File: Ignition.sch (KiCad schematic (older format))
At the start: 16 parts, among them Q1 Q_PMOS_GDS, Q2 Q_NMOS_GDS, Q3 Q_NMOS_GDS, Q4 Q_NMOS_GDS, Q5 Q_PMOS_GDS, Q6 Q_PMOS_GDS

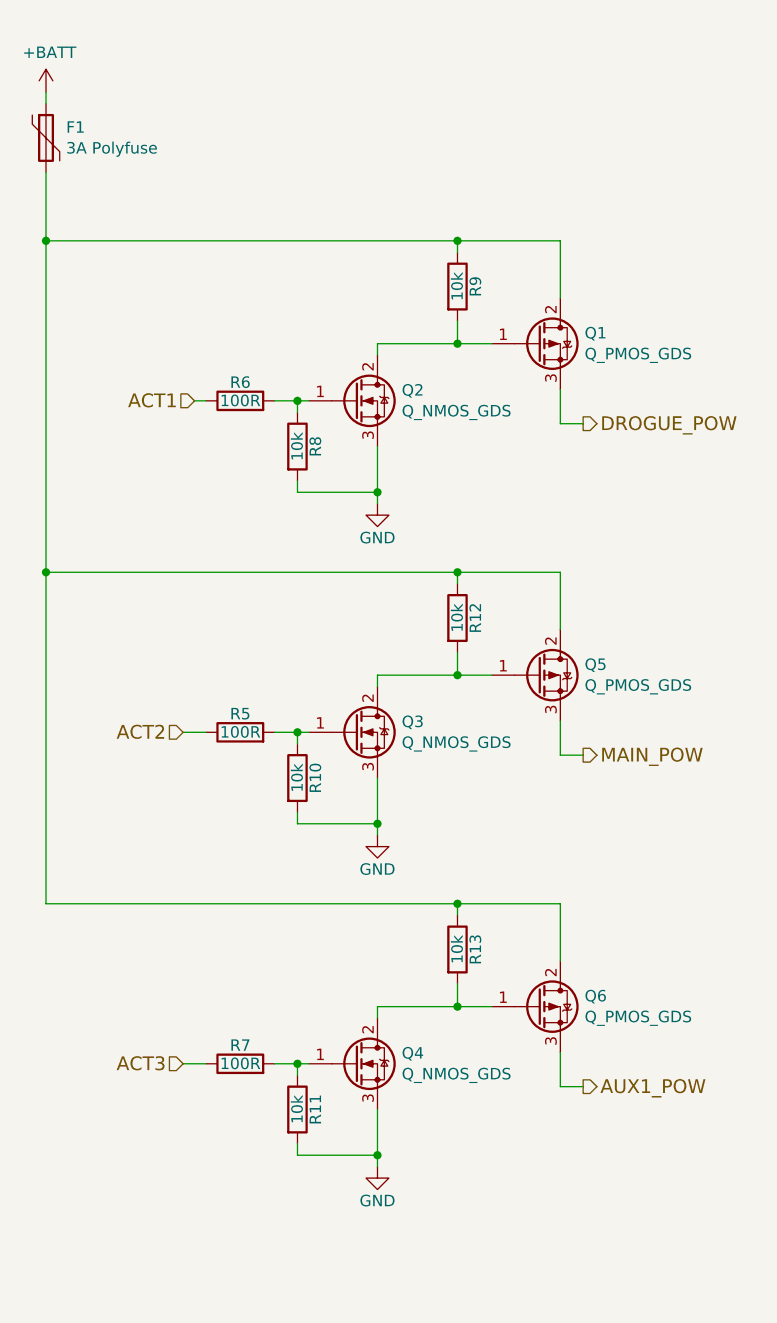
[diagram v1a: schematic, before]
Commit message: Added 10R series termination resistors to high-speed digital lines Added reverse-power protection diode Added ADC filter capacitors Added I2C pullups Added individual polyfuses to pyro drivers Changed UBSEDS logo to smaller variant Reduced LED resistors to 470R Reduced most SMD footprints to 0603 Minor schematic cleanup
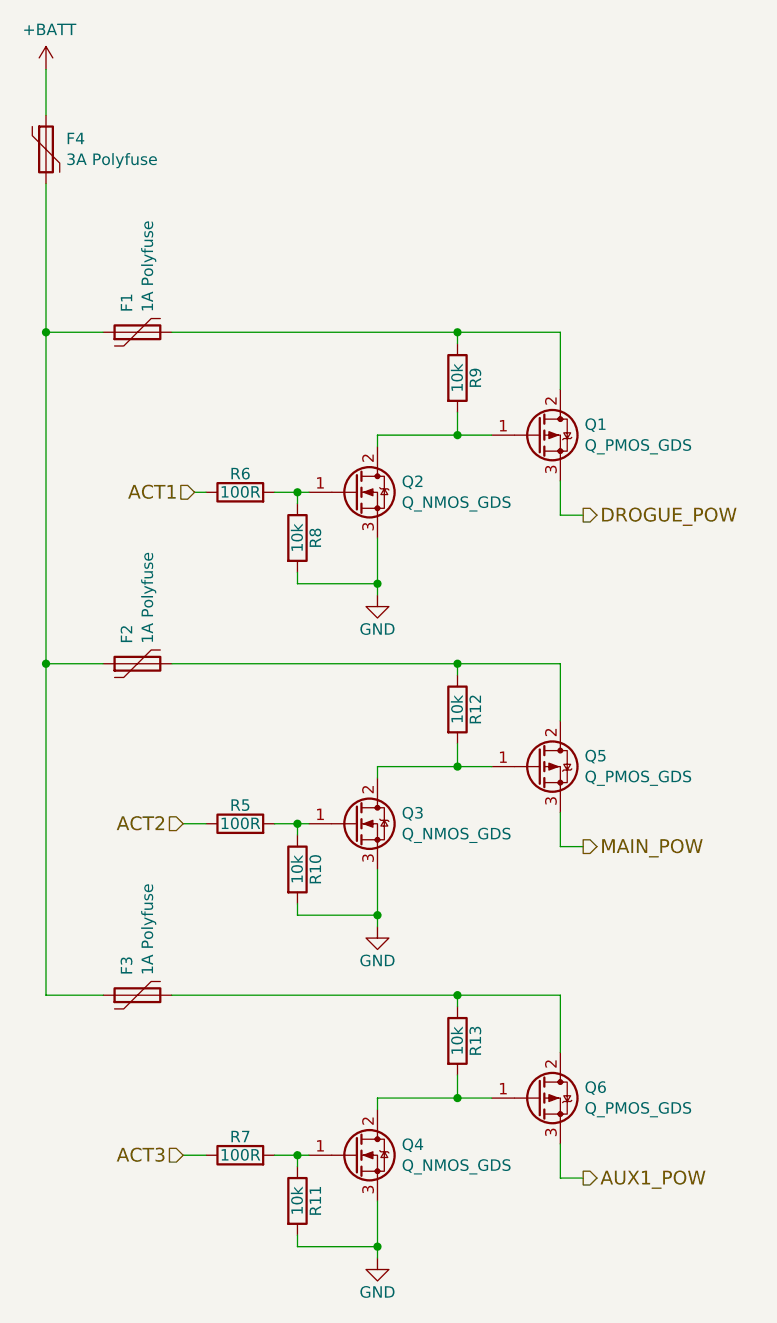
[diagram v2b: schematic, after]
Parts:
- added F2, F3: 1A Polyfuse, Fuse:Fuse_1206_3216Metric_Pad1.42x1.75mm_HandSolder, symbol Device:Polyfuse
- added F4: 3A Polyfuse, Fuse:Fuse_1206_3216Metric_Pad1.42x1.75mm_HandSolder, symbol Device:Polyfuse
- F1: value 3A Polyfuse -> 1A Polyfuse
- R10, R11, R12, R13, R5, R6, R7, R8, R9: footprint Resistor_SMD:R_1206_3216Metric_Pad1.42x1.75mm_HandSolder -> Resistor_SMD:R_0603_1608Metric_Pad1.05x0.95mm_HandSolder
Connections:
- net +BATT: now also F4.1; no longer F1.1
- new net: F1.2, Q1.2 (D), R9.1
- new net: F1.1, F2.1, F3.1, F4.2
- new net: F2.2, Q5.2 (D), R12.1
- new net: F3.2, Q6.2 (D), R13.1
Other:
- moved on the sheet: Q1, Q2, Q3, Q4, Q5, Q6, R10, R11, R12, R13, R5, R6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

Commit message: Routing complete Removed some test points (couldn't easily place)
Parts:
- removed Q2, Q3, Q4: Q_NMOS_GDS, Package_TO_SOT_SMD:SOT-23, symbol Device:Q_NMOS_GDS
- added Q2, Q3, Q4: 2N7002, Package_TO_SOT_SMD:SOT-23, symbol Transistor_FET:2N7002
- Q1, Q5, Q6: value Q_PMOS_GDS -> DMP3099; symbol Device:Q_PMOS_GDS -> Device:Q_PMOS_GSD
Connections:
- net GND: now also Q2.2 (S), Q3.2 (S), Q4.2 (S)
- net at Q1.1 (G), R9.2: now also Q2.3 (D)
- net at R6.2, R8.1: now also Q2.1 (G)
- net at Q5.1 (G), R12.2: now also Q3.3 (D)
- net at R10.1, R5.2: now also Q3.1 (G)
- net at Q6.1 (G), R13.2: now also Q4.3 (D)
- net at R11.1, R7.2: now also Q4.1 (G)
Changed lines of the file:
@@
-	1    0    0    -1
-$EndComp
-$Comp
-L Device:Q_PMOS_GDS Q1
-U 1 1 5E75362F
-P 5850 2600
-F 0 "Q1" H 6056 2646 50  0000 L CNN
-F 1 "Q_PMOS_GDS" H 6056 2555 50  0000 L CNN
-F 2 "Package_TO_SOT_SMD:SOT-23" H 6050 2700 50  0001 C CNN
-F 3 "~" H 5850 2600 50  0001 C CNN
-	1    5850 2600
 	1    0    0    -1
 $EndComp
@@
 Text HLabel 4350 2850 0    60   Input ~ 0
 ACT1
-$Comp
-L Device:Q_NMOS_GDS Q2
-U 1 1 5ED9D4A9
-P 5050 2850
-F 0 "Q2" H 5256 2896 50  0000 L CNN
-F 1 "Q_NMOS_GDS" H 5256 2805 50  0000 L CNN
-F 2 "Package_TO_SOT_SMD:SOT-23" H 5250 2950 50  0001 C CNN
-F 3 "~" H 5050 2850 50  0001 C CNN
-	1    5050 2850
-	1    0    0    -1
-$EndComp
 Wire Wire Line
 	5150 2600 5150 2650
@@
 $EndComp
 $Comp
-L Device:Q_PMOS_GDS Q5
+L Device:Q_PMOS_GSD Q5
 U 1 1 5E4C3E16
 P 5850 4050
 F 0 "Q5" H 6056 4096 50  0000 L CNN
-F 1 "Q_PMOS_GDS" H 6056 4005 50  0000 L CNN
+F 1 "DMP3099" H 6056 4005 50  0000 L CNN
 F 2 "Package_TO_SOT_SMD:SOT-23" H 6050 4150 50  0001 C CNN
 F 3 "~" H 5850 4050 50  0001 C CNN
 	1    5850 4050
-	1    0    0    -1
+	1    0    0    1
 $EndComp
 Wire Wire Line
@@
 	1    4550 4300
 	0    -1   -1   0
-$EndComp
-$Comp
-L Device:Q_NMOS_GDS Q3
-U 1 1 5E4C3E2C
-P 5050 4300
-F 0 "Q3" H 5256 4346 50  0000 L CNN
-F 1 "Q_NMOS_GDS" H 5256 4255 50  0000 L CNN
-F 2 "Package_TO_SOT_SMD:SOT-23" H 5250 4400 50  0001 C CNN
-F 3 "~" H 5050 4300 50  0001 C CNN
-	1    5050 4300
-	1    0    0    -1
 $EndComp
 Wire Wire Line
@@
 $EndComp
 $Comp
-L Device:Q_PMOS_GDS Q6
+L Device:Q_PMOS_GSD Q6
 U 1 1 5E4D9D25
 P 5850 5500
 F 0 "Q6" H 6056 5546 50  0000 L CNN
-F 1 "Q_PMOS_GDS" H 6056 5455 50  0000 L CNN
+F 1 "DMP3099" H 6056 5455 50  0000 L CNN
 F 2 "Package_TO_SOT_SMD:SOT-23" H 6050 5600 50  0001 C CNN
 F 3 "~" H 5850 5500 50  0001 C CNN
 	1    5850 5500
-	1    0    0    -1
+	1    0    0    1
 $EndComp
 Wire Wire Line
@@
 	1    4550 5750
 	0    -1   -1   0
-$EndComp
-$Comp
-L Device:Q_NMOS_GDS Q4
-U 1 1 5E4D9D3A
-P 5050 5750
-F 0 "Q4" H 5256 5796 50  0000 L CNN
-F 1 "Q_NMOS_GDS" H 5256 5705 50  0000 L CNN
-F 2 "Package_TO_SOT_SMD:SOT-23" H 5250 5850 50  0001 C CNN
-F 3 "~" H 5050 5750 50  0001 C CNN
-	1    5050 5750
-	1    0    0    -1
 $EndComp
 Wire Wire Line
@@
 Wire Wire Line
 	3700 1500 3700 2150
+$Comp
+L Transistor_FET:2N7002 Q2
+U 1 1 5E2FF20A
+P 5050 2850
+F 0 "Q2" H 5254 2896 50  0000 L CNN
+F 1 "2N7002" H 5254 2805 50  0000 L CNN
+F 2 "Package_TO_SOT_SMD:SOT-23" H 5250 2775 50  0001 L CIN
+F 3 "https://www.fairchildsemi.com/datasheets/2N/2N7002.pdf" H 5050 2850 50  0001 L CNN
+	1    5050 2850
+	1    0    0    -1
+$EndComp
+$Comp
+L Device:Q_PMOS_GSD Q1
+U 1 1 5E75362F
+P 5850 2600
+F 0 "Q1" H 6056 2646 50  0000 L CNN
+F 1 "DMP3099" H 6056 2555 50  0000 L CNN
+F 2 "Package_TO_SOT_SMD:SOT-23" H 6050 2700 50  0001 C CNN
+F 3 "~" H 5850 2600 50  0001 C CNN
+	1    5850 2600
+	1    0    0    1
+$EndComp
+$Comp
+L Transistor_FET:2N7002 Q3
+U 1 1 5E30C830
+P 5050 4300
+F 0 "Q3" H 5254 4346 50  0000 L CNN
+F 1 "2N7002" H 5254 4255 50  0000 L CNN
+F 2 "Package_TO_SOT_SMD:SOT-23" H 5250 4225 50  0001 L CIN
+F 3 "https://www.fairchildsemi.com/datasheets/2N/2N7002.pdf" H 5050 4300 50  0001 L CNN
+	1    5050 4300
+	1    0    0    -1
+$EndComp
+$Comp
+L Transistor_FET:2N7002 Q4
+U 1 1 5E310752
+P 5050 5750
+F 0 "Q4" H 5254 5796 50  0000 L CNN
+F 1 "2N7002" H 5254 5705 50  0000 L CNN
+F 2 "Package_TO_SOT_SMD:SOT-23" H 5250 5675 50  0001 L CIN
+F 3 "https://www.fairchildsemi.com/datasheets/2N/2N7002.pdf" H 5050 5750 50  0001 L CNN
+	1    5050 5750
+	1    0    0    -1
+$EndComp
 $EndSCHEMATC
